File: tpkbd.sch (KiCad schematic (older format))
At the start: 20 parts, among them CON1 AVR-ISP-6, J1 CONN_01X02, J2 CONN_01X01, J3 USB_OTG, J4 CONN_02X20, J5 CONN_01X04, J6 GS2, U1 ATMEGA8515-16AU, U2 AP111733, Y1 Crystal_GND24

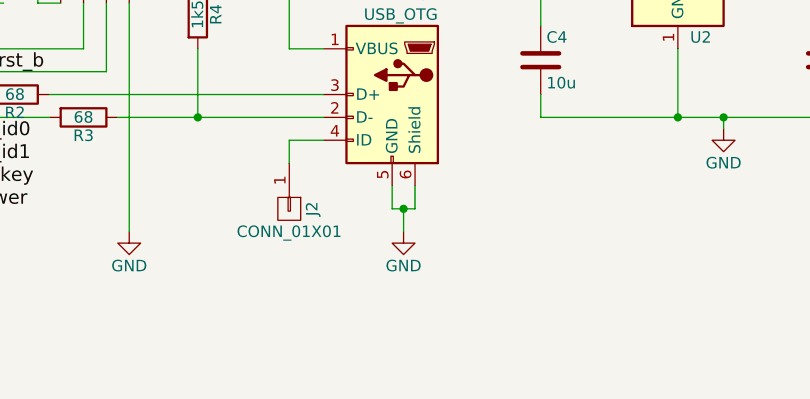
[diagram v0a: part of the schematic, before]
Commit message: added a LED
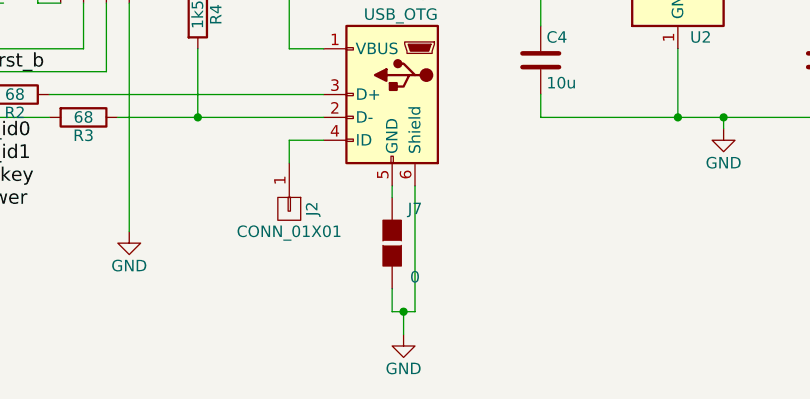
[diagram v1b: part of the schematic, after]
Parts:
- added J7: 0, Capacitors_SMD:C_0402, symbol GS2
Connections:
- net GND: now also J7.2 (G2); no longer J3.5 (GND)
- new net: J3.5 (GND), J7.1 (G1)
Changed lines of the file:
@@
 L GND #PWR02
 U 1 1 59BAADDC
-P 6650 6100
-F 0 "#PWR02" H 6650 5850 50  0001 C CNN
-F 1 "GND" H 6650 5950 50  0000 C CNN
-F 2 "" H 6650 6100 50  0001 C CNN
-F 3 "" H 6650 6100 50  0001 C CNN
-	1    6650 6100
+P 6650 6550
+F 0 "#PWR02" H 6650 6300 50  0001 C CNN
+F 1 "GND" H 6650 6400 50  0000 C CNN
+F 2 "" H 6650 6550 50  0001 C CNN
+F 3 "" H 6650 6550 50  0001 C CNN
+	1    6650 6550
 	1    0    0    -1
 $EndComp
@@
 	6150 5700 6300 5700
 Wire Wire Line
-	6600 5900 6600 6000
-Wire Wire Line
-	6600 6000 6700 6000
-Wire Wire Line
-	6650 6000 6650 6100
-Wire Wire Line
-	6700 6000 6700 5900
-Connection ~ 6650 6000
+	6600 6350 6600 6450
+Wire Wire Line
+	6600 6450 6700 6450
+Wire Wire Line
+	6650 6450 6650 6550
+Wire Wire Line
+	6700 6450 6700 5900
+Connection ~ 6650 6450
 Wire Wire Line
 	6150 5300 6300 5300
@@
 Wire Wire Line
 	6000 3600 6150 3600
+$Comp
+L GS2 J7
+U 1 1 59BB22E9
+P 6600 6150
+F 0 "J7" H 6700 6300 50  0000 C CNN
+F 1 "0" H 6700 6001 50  0000 C CNN
+F 2 "Capacitors_SMD:C_0402" V 6674 6150 50  0001 C CNN
+F 3 "" H 6600 6150 50  0001 C CNN
+	1    6600 6150
+	1    0    0    -1
+$EndComp
+Wire Wire Line
+	6600 5900 6600 5950
 $EndSCHEMATC

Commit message: cleanup
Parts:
- removed CON1: AVR-ISP-6, Pin_Headers:Pin_Header_Straight_2x03, symbol AVR-ISP-6
- added D1: LED, KX14:PLCC4, symbol LED_Dual_AACC
- added J?: CONN_02X10, symbol CONN_02X10
- added R6, R7, R8: R, Resistors_SMD:R_0603_HandSoldering, symbol R
- C1, C2: footprint Capacitors_SMD:C_0805_HandSoldering -> Capacitors_SMD:C_0603_HandSoldering
- C3: footprint Capacitors_SMD:C_0402 -> Capacitors_SMD:C_0603_HandSoldering
- J2: footprint Pin_Headers:Pin_Header_Straight_1x01 -> KX14:Pins1x1
- J4: value CONN_02X20 -> CONN_02X21; symbol CONN_02X20 -> CONN_02X21
- R1, R2, R3, R4, R5: footprint Resistors_SMD:R_0805_HandSoldering -> Resistors_SMD:R_0603_HandSoldering
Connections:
- net +3V3: now also J?.2 (P2), R6.1; no longer J5.1 (P1)
- net +5V: now also J5.1 (P1)
- net B5: now also J?.4 (P4)
- net B6: now also J?.6 (P6)
- net B7: now also J?.8 (P8)
- net GND: now also J4.41 (P41), J?.12 (P12), R8.2
- net RST: now also J?.10 (P10)
- net kb_id0: now also R7.1; no longer U1.10 ((XCK)PD4)
- net at R3.2: now also U1.10 ((XCK)PD4); no longer U1.9 ((INT1)PD3)
- new net: D1.2 (A2), R6.2
- new net: D1.3 (K1), R8.1
- new net led: D1.1 (A1), D1.4 (K2), R7.2, U1.9 ((INT1)PD3)
- no-connect marks 4 -> 19
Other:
- moved on the sheet: J7, R3

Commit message: cleanup2
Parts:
- removed J1: CONN_01X02, Buttons_Switches_SMD:SW_SPST_FSMSM, symbol CONN_01X02
- removed J?: CONN_02X10, symbol CONN_02X10
- added J8: CONN_01X05, KX14:Pins_1x5, symbol CONN_01X05
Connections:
- net B5: now also J8.5 (P5)
- net B6: now also J8.4 (P4)
- net B7: now also J8.3 (P3)
- net GND: now also J8.1 (P1)
- net RST: now also J8.2 (P2)
- no-connect marks 19 -> 5
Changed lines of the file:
@@
-$EndComp
-$Comp
-L CONN_01X02 J1
-U 1 1 59BAB43F
-P 1900 2300
-F 0 "J1" H 1900 2450 50  0000 C CNN
-F 1 "CONN_01X02" V 2000 2300 50  0000 C CNN
-F 2 "Buttons_Switches_SMD:SW_SPST_FSMSM" H 1900 2300 50  0001 C CNN
-F 3 "" H 1900 2300 50  0001 C CNN
-	1    1900 2300
-	0    -1   -1   0
 $EndComp
 $Comp
@@
 Text Label 2400 2600 0    60   ~ 0
 RST
-Text Label 10550 3050 2    60   ~ 0
+Text Label 10550 2950 2    60   ~ 0
 RST
 Text Label 7050 2500 0    60   ~ 0
@@
 Connection ~ 6150 5000
 Wire Wire Line
-	10550 3050 10100 3050
+	10550 2950 10100 2950
+Wire Wire Line
+	10550 2750 10100 2750
 Wire Wire Line
 	10550 2850 10100 2850
 Wire Wire Line
-	10550 2950 10100 2950
-Wire Wire Line
 	10100 2650 10550 2650
 Wire Wire Line
-	10100 2750 10550 2750
-Wire Wire Line
-	10100 3150 10550 3150
+	10100 3050 10550 3050
 Wire Wire Line
 	7350 2500 7050 2500
@@
 Wire Wire Line
 	4550 5100 4900 5100
+Text Label 10550 2750 2    60   ~ 0
+MISO
 Text Label 10550 2850 2    60   ~ 0
-MISO
-Text Label 10550 2950 2    60   ~ 0
 SCK
-Text Label 10550 2750 0    60   ~ 0
+Text Label 10550 2650 0    60   ~ 0
 MOSI
 $Comp
 L GND #PWR014
 U 1 1 59BAD155
-P 10550 3250
-F 0 "#PWR014" H 10550 3000 50  0001 C CNN
-F 1 "GND" H 10550 3100 50  0000 C CNN
-F 2 "" H 10550 3250 50  0001 C CNN
-F 3 "" H 10550 3250 50  0001 C CNN
-	1    10550 3250
-	1    0    0    -1
-$EndComp
-Wire Wire Line
-	10550 3150 10550 3250
+P 10550 3150
+F 0 "#PWR014" H 10550 2900 50  0001 C CNN
+F 1 "GND" H 10550 3000 50  0000 C CNN
+F 2 "" H 10550 3150 50  0001 C CNN
+F 3 "" H 10550 3150 50  0001 C CNN
+	1    10550 3150
+	1    0    0    -1
+$EndComp
+Wire Wire Line
+	10550 3050 10550 3150
 Text Label 5100 4100 0    60   ~ 0
 MISO
@@
 	6900 4850 6900 5000
 Connection ~ 6900 5000
-$Comp
-L +3V3 #PWR017
-U 1 1 59BADCC0
-P 10550 2500
-F 0 "#PWR017" H 10550 2350 50  0001 C CNN
-F 1 "+3V3" H 10550 2640 50  0000 C CNN
-F 2 "" H 10550 2500 50  0001 C CNN
-F 3 "" H 10550 2500 50  0001 C CNN
-	1    10550 2500
-	1    0    0    -1
-$EndComp
-Wire Wire Line
-	10550 2650 10550 2500
 Wire Wire Line
 	4100 2200 4100 2000
@@
 	5350 5400 5350 5100
 $Comp
-L GND #PWR018
+L GND #PWR017
 U 1 1 59BAE839
 P 5450 6100
-F 0 "#PWR018" H 5450 5850 50  0001 C CNN
+F 0 "#PWR017" H 5450 5850 50  0001 C CNN
 F 1 "GND" H 5450 5950 50  0000 C CNN
 F 2 "" H 5450 6100 50  0001 C CNN
@@
 	5050 5100 5150 5100
 $Comp
-L PWR_FLAG #FLG019
+L PWR_FLAG #FLG018
 U 1 1 59BAEACE
 P 9100 5450
-F 0 "#FLG019" H 9100 5525 50  0001 C CNN
+F 0 "#FLG018" H 9100 5525 50  0001 C CNN
 F 1 "PWR_FLAG" H 9100 5600 50  0000 C CNN
 F 2 "" H 9100 5450 50  0001 C CNN
@@
 Connection ~ 8500 5600
 $Comp
-L PWR_FLAG #FLG020
+L PWR_FLAG #FLG019
 U 1 1 59BAEC2F
 P 9450 4900
-F 0 "#FLG020" H 9450 4975 50  0001 C CNN
+F 0 "#FLG019" H 9450 4975 50  0001 C CNN
 F 1 "PWR_FLAG" H 9450 5050 50  0000 C CNN
 F 2 "" H 9450 4900 50  0001 C CNN
@@
 $EndComp
 $Comp
-L GND #PWR021
+L GND #PWR020
 U 1 1 59BAF57F
 P 1850 3800
-F 0 "#PWR021" H 1850 3550 50  0001 C CNN
+F 0 "#PWR020" H 1850 3550 50  0001 C CNN
 F 1 "GND" H 1850 3650 50  0000 C CNN
 F 2 "" H 1850 3800 50  0001 C CNN
@@
 	1850 3300 1900 3300
 $Comp
-L GND #PWR022
+L GND #PWR021
 U 1 1 59BAF671
 P 2350 3800
-F 0 "#PWR022" H 2350 3550 50  0001 C CNN
+F 0 "#PWR021" H 2350 3550 50  0001 C CNN
 F 1 "GND" H 2350 3650 50  0000 C CNN
 F 2 "" H 2350 3800 50  0001 C CNN
@@
 	750  6250 750  6350
 $Comp
-L GND #PWR023
+L GND #PWR022
 U 1 1 59BB2E4B
 P 1350 7350
-F 0 "#PWR023" H 1350 7100 50  0001 C CNN
+F 0 "#PWR022" H 1350 7100 50  0001 C CNN
 F 1 "GND" H 1350 7200 50  0000 C CNN
 F 2 "" H 1350 7350 50  0001 C CNN
@@
 	1350 6950 1350 7350
 $Comp
-L PWR_FLAG #FLG024
+L PWR_FLAG #FLG023
 U 1 1 59BB3276
 P 7050 5850
-F 0 "#FLG024" H 7050 5925 50  0001 C CNN
+F 0 "#FLG023" H 7050 5925 50  0001 C CNN
 F 1 "PWR_FLAG" H 7050 6000 50  0000 C CNN
 F 2 "" H 7050 5850 50  0001 C CNN
@@
 NoConn ~ 7850 3700
 $Comp
-L +3V3 #PWR025
+L +3V3 #PWR024
 U 1 1 59BBC4D0
 P 750 5800
-F 0 "#PWR025" H 750 5650 50  0001 C CNN
+F 0 "#PWR024" H 750 5650 50  0001 C CNN
 F 1 "+3V3" H 750 5940 50  0000 C CNN
 F 2 "" H 750 5800 50  0001 C CNN
@@
 $EndComp
 $Comp
-L +5V #PWR026
+L +5V #PWR025
 U 1 1 59BBCA91
 P 5050 4700
-F 0 "#PWR026" H 5050 4550 50  0001 C CNN
+F 0 "#PWR025" H 5050 4550 50  0001 C CNN
 F 1 "+5V" H 5050 4840 50  0000 C CNN
 F 2 "" H 5050 4700 50  0001 C CNN
@@
 $EndComp
 $Comp
-L CONN_02X10 J?
-U 1 1 59BBD507
-P 9850 3100
-F 0 "J?" H 9850 3650 50  0000 C CNN
-F 1 "CONN_02X10" V 9850 3100 50  0000 C CNN
-F 2 "" H 9850 1900 50  0001 C CNN
-F 3 "" H 9850 1900 50  0001 C CNN
-	1    9850 3100
-	1    0    0    -1
-$EndComp
-NoConn ~ 9600 2650
-NoConn ~ 9600 2750
-NoConn ~ 9600 2850
-NoConn ~ 9600 2950
-NoConn ~ 9600 3050
-NoConn ~ 9600 3150
-NoConn ~ 9600 3250
-NoConn ~ 9600 3350
-NoConn ~ 9600 3450
-NoConn ~ 9600 3550
-NoConn ~ 10100 3250
-NoConn ~ 10100 3350
-NoConn ~ 10100 3450
-NoConn ~ 10100 3550
+L CONN_01X05 J8
+U 1 1 59BBF4F8
+P 9900 2850
+F 0 "J8" H 9900 3200 50  0000 C CNN
+F 1 "CONN_01X05" V 10000 2850 50  0000 C CNN
+F 2 "KX14:Pins_1x5" H 9900 2850 50  0001 C CNN
+F 3 "" H 9900 2850 50  0001 C CNN
+	1    9900 2850
+	-1   0    0    1
+$EndComp
 $EndSCHEMATC

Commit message: schema: add values of components
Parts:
- added J1: mount_2, KX14:mount_m2, symbol CONN_01X01
- added J9: mount_1, KX14:mount_m2, symbol CONN_01X01
- C1, C2: value C -> 33p
- R1: value 10k -> 1k5
- R6: value R -> 22
- R7: value R -> 1k5
- R8: value R -> 120
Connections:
- net GND: now also J1.1 (P1), J9.1 (P1)
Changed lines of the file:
@@
 P 1600 3100
 F 0 "C1" H 1625 3200 50  0000 L CNN
-F 1 "C" H 1625 3000 50  0000 L CNN
+F 1 "33p" H 1625 3000 50  0000 L CNN
 F 2 "Capacitors_SMD:C_0603_HandSoldering" H 1638 2950 50  0001 C CNN
 F 3 "" H 1600 3100 50  0001 C CNN
@@
 P 1600 3500
 F 0 "C2" H 1625 3600 50  0000 L CNN
-F 1 "C" H 1625 3400 50  0000 L CNN
+F 1 "33p" H 1625 3400 50  0000 L CNN
 F 2 "Capacitors_SMD:C_0603_HandSoldering" H 1638 3350 50  0001 C CNN
 F 3 "" H 1600 3500 50  0001 C CNN
@@
 P 2300 2350
 F 0 "R1" V 2380 2350 50  0000 C CNN
-F 1 "10k" V 2300 2350 50  0000 C CNN
+F 1 "1k5" V 2300 2350 50  0000 C CNN
 F 2 "Resistors_SMD:R_0603_HandSoldering" V 2230 2350 50  0001 C CNN
 F 3 "" H 2300 2350 50  0001 C CNN
@@
 P 750 6100
 F 0 "R6" V 830 6100 50  0000 C CNN
-F 1 "R" V 750 6100 50  0000 C CNN
+F 1 "22" V 750 6100 50  0000 C CNN
 F 2 "Resistors_SMD:R_0603_HandSoldering" V 680 6100 50  0001 C CNN
 F 3 "" H 750 6100 50  0001 C CNN
@@
 P 1800 6450
 F 0 "R7" V 1880 6450 50  0000 C CNN
-F 1 "R" V 1800 6450 50  0000 C CNN
+F 1 "1k5" V 1800 6450 50  0000 C CNN
 F 2 "Resistors_SMD:R_0603_HandSoldering" V 1730 6450 50  0001 C CNN
 F 3 "" H 1800 6450 50  0001 C CNN
@@
 P 1350 6800
 F 0 "R8" V 1430 6800 50  0000 C CNN
-F 1 "R" V 1350 6800 50  0000 C CNN
+F 1 "120" V 1350 6800 50  0000 C CNN
 F 2 "Resistors_SMD:R_0603_HandSoldering" V 1280 6800 50  0001 C CNN
 F 3 "" H 1350 6800 50  0001 C CNN
@@
 	-1   0    0    1
 $EndComp
+$Comp
+L CONN_01X01 J1
+U 1 1 59BD1853
+P 9950 1100
+F 0 "J1" H 9950 1200 50  0000 C CNN
+F 1 "mount_2" V 10050 1100 50  0000 C CNN
+F 2 "KX14:mount_m2" H 9950 1100 50  0001 C CNN
+F 3 "" H 9950 1100 50  0001 C CNN
+	1    9950 1100
+	1    0    0    -1
+$EndComp
+$Comp
+L CONN_01X01 J9
+U 1 1 59BD18E7
+P 9950 1550
+F 0 "J9" H 9950 1650 50  0000 C CNN
+F 1 "mount_1" V 10050 1550 50  0000 C CNN
+F 2 "KX14:mount_m2" H 9950 1550 50  0001 C CNN
+F 3 "" H 9950 1550 50  0001 C CNN
+	1    9950 1550
+	1    0    0    -1
+$EndComp
+$Comp
+L GND #PWR026
+U 1 1 59BD19A3
+P 9750 1550
+F 0 "#PWR026" H 9750 1300 50  0001 C CNN
+F 1 "GND" H 9750 1400 50  0000 C CNN
+F 2 "" H 9750 1550 50  0001 C CNN
+F 3 "" H 9750 1550 50  0001 C CNN
+	1    9750 1550
+	1    0    0    -1
+$EndComp
+$Comp
+L GND #PWR027
+U 1 1 59BD1BC7
+P 9750 1100
+F 0 "#PWR027" H 9750 850 50  0001 C CNN
+F 1 "GND" H 9750 950 50  0000 C CNN
+F 2 "" H 9750 1100 50  0001 C CNN
+F 3 "" H 9750 1100 50  0001 C CNN
+	1    9750 1100
+	1    0    0    -1
+$EndComp
 $EndSCHEMATC
